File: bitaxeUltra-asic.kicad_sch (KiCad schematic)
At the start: 2 parts, among them J1 Conn_01x03_Pin, J2 Conn_01x03_Pin

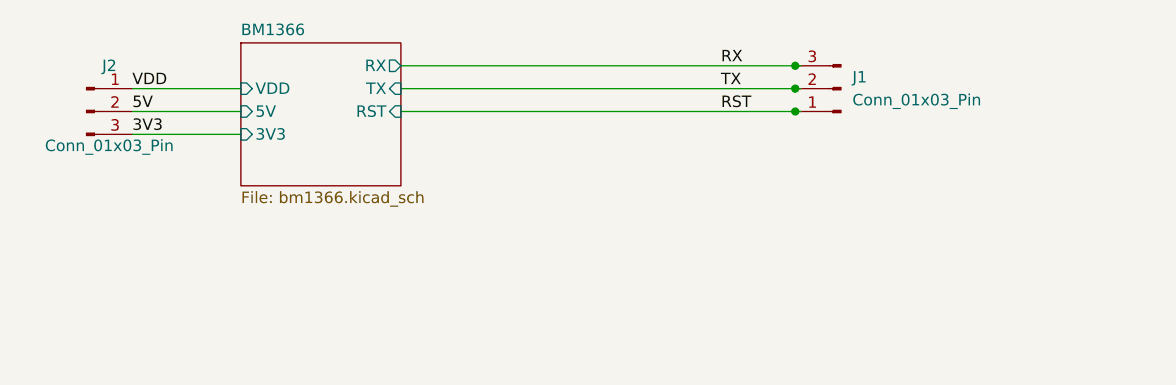
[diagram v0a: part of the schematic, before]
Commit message: revert  to 4 layer-board routing
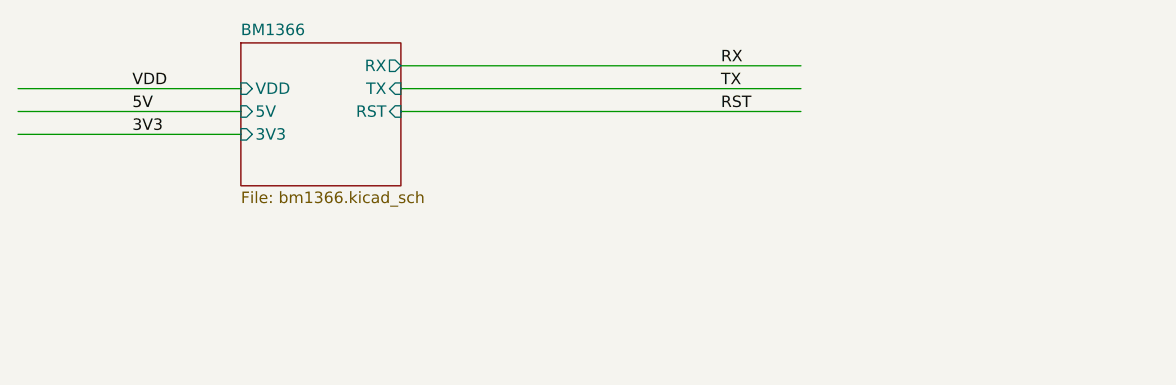
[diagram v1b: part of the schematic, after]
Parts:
- removed J1: Conn_01x03_Pin, Connector_JST:JST_PH_B3B-PH-K_1x03_P2.00mm_Vertical, symbol Connector:Conn_01x03_Pin
- removed J2: Conn_01x03_Pin, Connector_Wire:SolderWire-0.5sqmm_1x03_P4.8mm_D0.9mm_OD2.3mm_Relief, symbol Connector:Conn_01x03_Pin
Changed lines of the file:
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@@
     (rev "203")
   )
-  (junction (at 173.99 74.93) (diameter 0) (color 0 0 0 0)
-  )
-  (junction (at 173.99 69.85) (diameter 0) (color 0 0 0 0)
-  )
-  (junction (at 173.99 72.39) (diameter 0) (color 0 0 0 0)
-  )
-  (wire (pts (xy 173.99 69.85) (xy 174.625 69.85))
+  (wire (pts (xy 87.63 72.39) (xy 112.395 72.39))
     (stroke (width 0) (type default))
   )
-  (wire (pts (xy 100.33 72.39) (xy 112.395 72.39))
+  (wire (pts (xy 130.175 72.39) (xy 174.625 72.39))
     (stroke (width 0) (type default))
   )
-  (wire (pts (xy 130.175 72.39) (xy 173.99 72.39))
+  (wire (pts (xy 87.63 77.47) (xy 112.395 77.47))
     (stroke (width 0) (type default))
   )
-  (wire (pts (xy 100.33 77.47) (xy 112.395 77.47))
+  (wire (pts (xy 87.63 74.93) (xy 112.395 74.93))
     (stroke (width 0) (type default))
   )
-  (wire (pts (xy 100.33 74.93) (xy 112.395 74.93))
+  (wire (pts (xy 130.175 69.85) (xy 174.625 69.85))
     (stroke (width 0) (type default))
   )
-  (wire (pts (xy 130.175 69.85) (xy 173.99 69.85))
-    (stroke (width 0) (type default))
-  )
-  (wire (pts (xy 173.99 74.93) (xy 174.625 74.93))
-    (stroke (width 0) (type default))
-  )
-  (wire (pts (xy 130.175 74.93) (xy 173.99 74.93))
-    (stroke (width 0) (type default))
-  )
-  (wire (pts (xy 173.99 72.39) (xy 174.625 72.39))
+  (wire (pts (xy 130.175 74.93) (xy 174.625 74.93))
     (stroke (width 0) (type default))
   )
@@
     (effects (font (size 1.27 1.27)) (justify left bottom))
   )
-  (symbol (lib_id "Connector:Conn_01x03_Pin") (at 95.25 74.93 0) (unit 1)
-    (in_bom yes) (on_board yes) (dnp no)
-    (property "Reference" "J2" (at 97.79 69.85 0)
-      (effects (font (size 1.27 1.27)))
-    )
-    (property "Value" "Conn_01x03_Pin" (at 97.79 78.74 0)
-      (effects (font (size 1.27 1.27)))
-    )
-    (property "Footprint" "Connector_Wire:SolderWire-0.5sqmm_1x03_P4.8mm_D0.9mm_OD2.3mm_Relief" (at 95.25 74.93 0)
-      (effects (font (size 1.27 1.27)) hide)
-    )
-    (property "Datasheet" "~" (at 95.25 74.93 0)
-      (effects (font (size 1.27 1.27)) hide)
-    )
-    (pin "1")
-    (pin "2")
-    (pin "3")
-    (instances
-      (project "bitaxeUltra-asic"
-        (path "/e63e39d7-6ac0-4ffd-8aa3-1841a4541b55"
-          (reference "J2") (unit 1)
-        )
-      )
-    )
-  )
   (symbol (lib_id "bitaxe:LOGO") (at 197.485 173.99 0) (unit 1)
     (in_bom yes) (on_board yes) (dnp no) (fields_autoplaced)
@@
         )
       )
-    )
-  )
-  (symbol (lib_id "Connector:Conn_01x03_Pin") (at 179.07 72.39 180) (unit 1)
-    (in_bom yes) (on_board yes) (dnp no) (fields_autoplaced)
-    (property "Reference" "J1" (at 180.34 71.12 0)
-      (effects (font (size 1.27 1.27)) (justify right))
-    )
-    (property "Value" "Conn_01x03_Pin" (at 180.34 73.66 0)
-      (effects (font (size 1.27 1.27)) (justify right))
-    )
-    (property "Footprint" "Connector_JST:JST_PH_B3B-PH-K_1x03_P2.00mm_Vertical" (at 179.07 72.39 0)
-      (effects (font (size 1.27 1.27)) hide)
-    )
-    (property "Datasheet" "~" (at 179.07 72.39 0)
-      (effects (font (size 1.27 1.27)) hide)
-    )
-    (property "LCSC" "C131339" (at 179.07 72.39 0)
-      (effects (font (size 1.27 1.27)) hide)
-    )
-    (pin "1")
-    (pin "2")
-    (pin "3")
-    (instances
-      (project "bitaxeUltra-asic"
-        (path "/e63e39d7-6ac0-4ffd-8aa3-1841a4541b55"
-          (reference "J1") (unit 1)
-        )
-      )
